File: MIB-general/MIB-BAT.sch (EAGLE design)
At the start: 19 parts, among them IC1 74LS14N, X1 MAB5SH, X2 MAB5SH

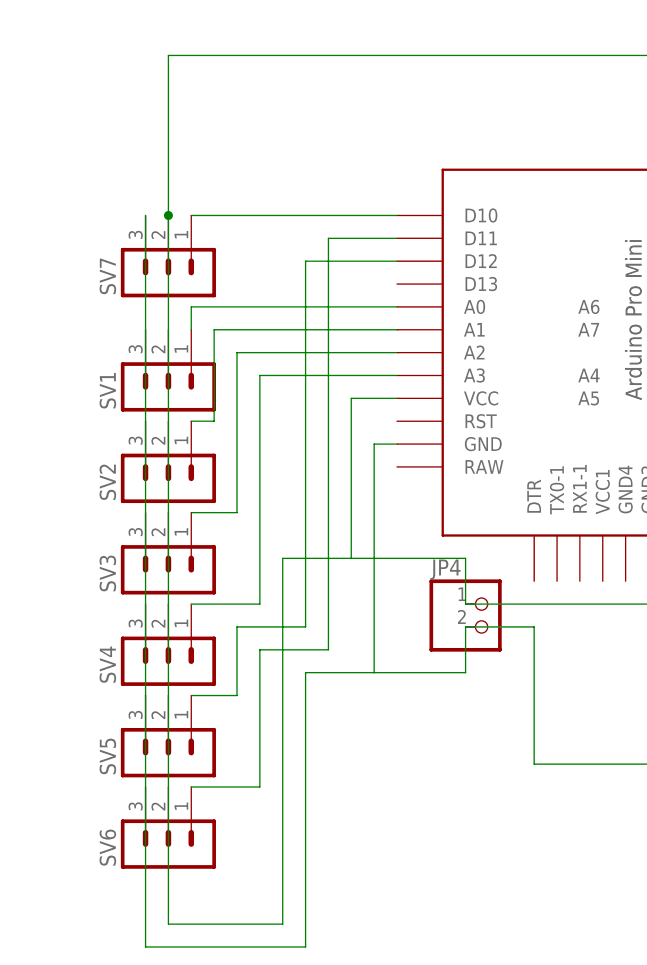
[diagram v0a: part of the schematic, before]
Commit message: Better version board with optional battery power supply
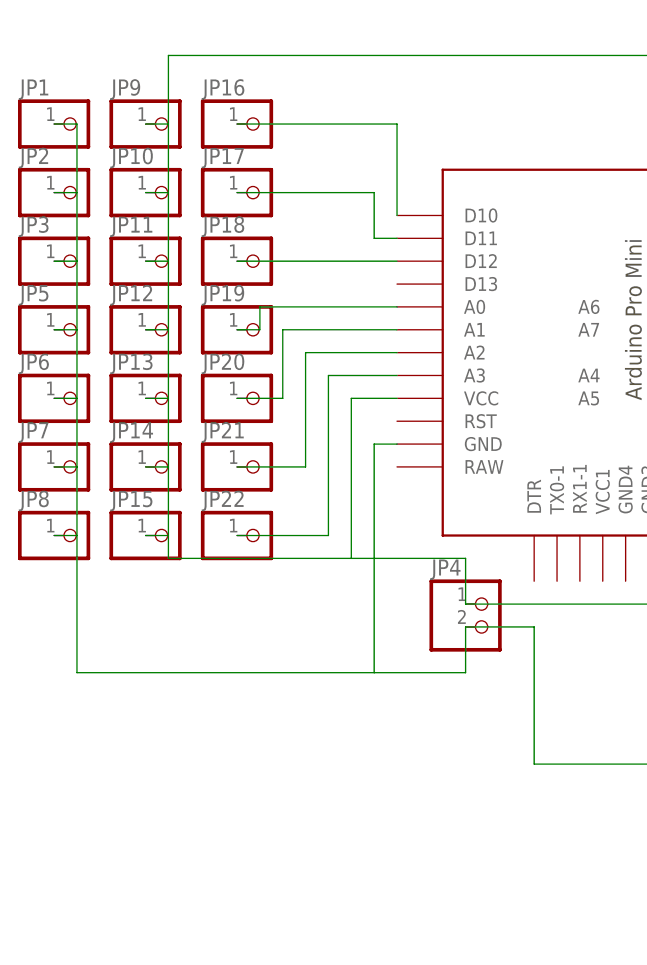
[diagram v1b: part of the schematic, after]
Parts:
- removed SV1, SV2, SV3, SV4, SV5, SV6, SV7: (no value), con-lstb:MA03-1
- added JP1, JP10, JP11, JP12, JP13, JP14, JP15, JP16, JP17, JP18, JP19, JP2, JP20, JP21, JP22, JP3, JP5, JP6, JP7, JP8, JP9: (no value), pinhead:PINHD-1X1
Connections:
- removed net N$9: IC1P.VCC, JP4.1, OK2.VCC, R2.1, R3.2, SV1.2, SV2.2, SV3.2, SV4.2, SV5.2, SV6.2, SV7.2, U$1.VCC
- new net N$29: JP21.1, U$1.A2
- net N$11: now also JP1.1, JP2.1, JP3.1, JP5.1, JP6.1, JP7.1, JP8.1; no longer SV1.3, SV2.3, SV3.3, SV4.3, SV5.3, SV6.3, SV7.3
- net N$13: now also JP16.1, U$1.D10; no longer SV2.1, U$1.A1
- net N$14: now also JP17.1, U$1.D11; no longer SV3.1, U$1.A2
- net N$15: now also IC1P.VCC, JP10.1, JP11.1, JP12.1, JP13.1, JP14.1, JP15.1, JP4.1, JP9.1, OK2.VCC, R2.1, R3.2, U$1.VCC; no longer SV4.1, U$1.A3
- net N$16: now also JP18.1, U$1.D12; no longer SV1.1, U$1.A0
- net N$18: now also JP19.1, U$1.A0; no longer SV5.1, U$1.D12
- net N$19: now also JP20.1, U$1.A1; no longer SV6.1, U$1.D11
- net N$30: now also JP22.1, U$1.A3; no longer SV7.1, U$1.D10

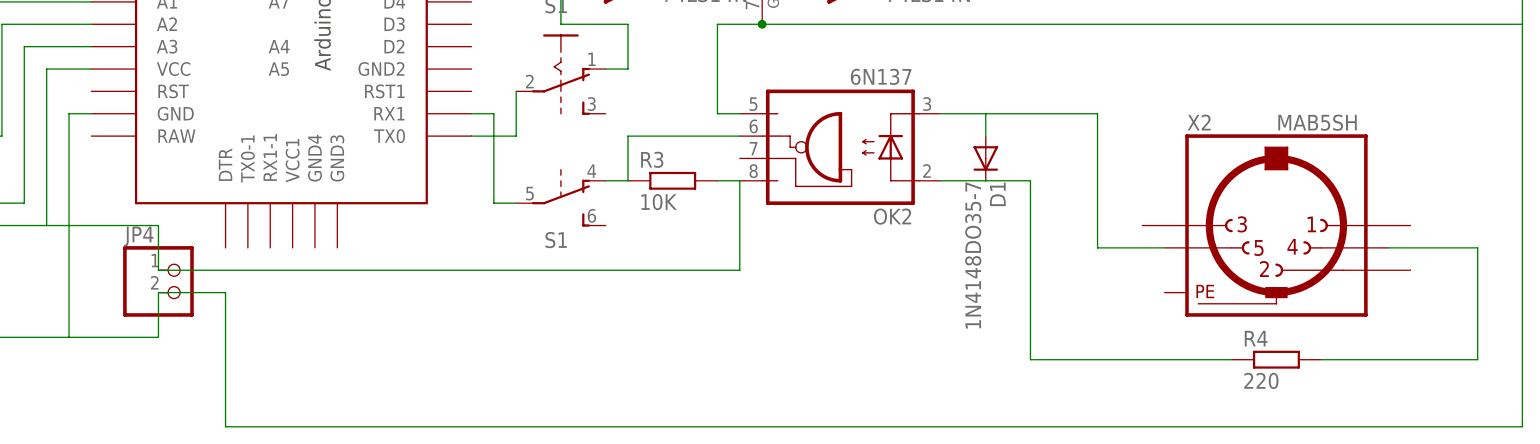
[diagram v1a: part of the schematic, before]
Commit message: New PCB layout enabling choice of optocoupler and makes the buffer optional.
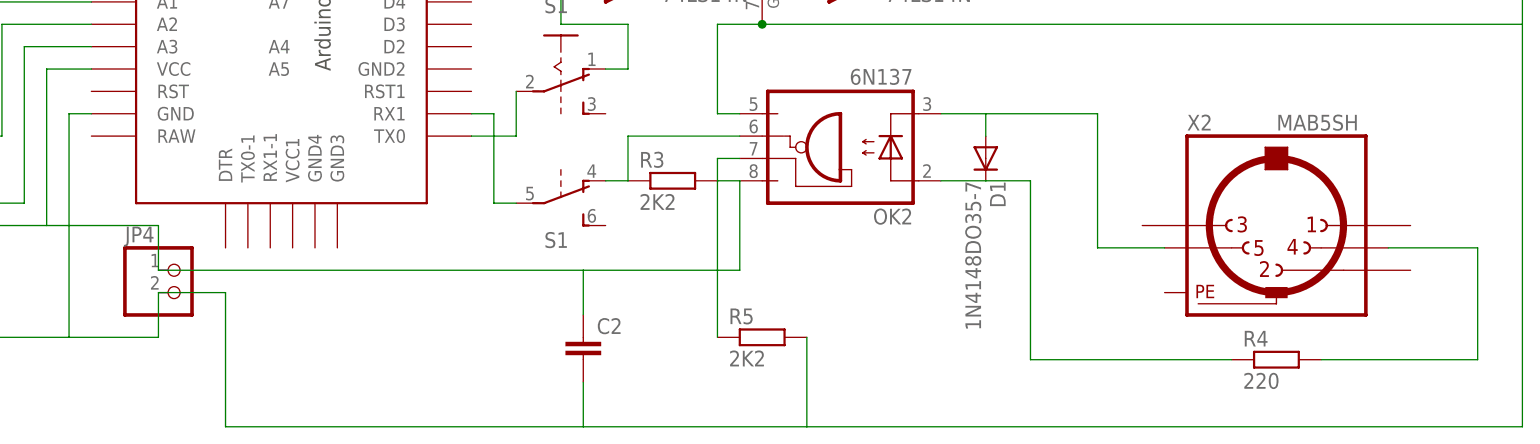
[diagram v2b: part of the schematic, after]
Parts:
- added C2: (no value), capacitor-wima:C7.5/3
- added R5: 2K2, rcl:R-EU_0207/10
- R3: value 10K -> 2K2
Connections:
- new net N$41: OK2.VE, R5.1
- net N$11: now also C2.2, R5.2
- net N$15: now also C2.1
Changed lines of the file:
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@@
 <part name="R1" library="rcl" deviceset="R-EU_" device="0207/10" value="220"/>
 <part name="R2" library="rcl" deviceset="R-EU_" device="0207/10" value="220"/>
-<part name="R3" library="rcl" deviceset="R-EU_" device="0207/10" value="10K"/>
+<part name="R3" library="rcl" deviceset="R-EU_" device="0207/10" value="2K2"/>
 <part name="R4" library="rcl" deviceset="R-EU_" device="0207/10" value="220"/>
 <part name="D1" library="diode" deviceset="1N4148" device="DO35-7"/>
@@
 <part name="JP21" library="pinhead" deviceset="PINHD-1X1" device=""/>
 <part name="JP22" library="pinhead" deviceset="PINHD-1X1" device=""/>
+<part name="C2" library="capacitor-wima" deviceset="C" device="7.5/3"/>
+<part name="R5" library="rcl" deviceset="R-EU_" device="0207/10" value="2K2"/>
 </parts>
 <sheets>
@@
 <instance part="JP21" gate="G$1" x="-7.62" y="40.64"/>
 <instance part="JP22" gate="G$1" x="-7.62" y="33.02"/>
+<instance part="C2" gate="G$1" x="63.5" y="17.78"/>
+<instance part="R5" gate="G$1" x="83.82" y="17.78"/>
 </instances>
 <busses>
@@
 <pinref part="X1" gate="G$1" pin="2"/>
 <wire x1="170.18" y1="53.34" x2="170.18" y2="7.62" width="0.1524" layer="91"/>
-<wire x1="170.18" y1="7.62" x2="22.86" y2="7.62" width="0.1524" layer="91"/>
+<wire x1="170.18" y1="7.62" x2="88.9" y2="7.62" width="0.1524" layer="91"/>
+<wire x1="88.9" y1="7.62" x2="63.5" y2="7.62" width="0.1524" layer="91"/>
+<wire x1="63.5" y1="7.62" x2="22.86" y2="7.62" width="0.1524" layer="91"/>
 <wire x1="22.86" y1="7.62" x2="22.86" y2="22.86" width="0.1524" layer="91"/>
 <wire x1="22.86" y1="22.86" x2="15.24" y2="22.86" width="0.1524" layer="91"/>
@@
 <pinref part="JP8" gate="G$1" pin="1"/>
 <wire x1="-30.48" y1="33.02" x2="-27.94" y2="33.02" width="0.1524" layer="91"/>
+<pinref part="C2" gate="G$1" pin="2"/>
+<wire x1="63.5" y1="12.7" x2="63.5" y2="7.62" width="0.1524" layer="91"/>
+<pinref part="R5" gate="G$1" pin="2"/>
+<wire x1="88.9" y1="17.78" x2="88.9" y2="7.62" width="0.1524" layer="91"/>
 </segment>
 </net>
@@
 </segment>
 </net>
-<net name="N$22" class="0">
+<net name="N$42" class="0">
 <segment>
 <pinref part="S1" gate="A" pin="O"/>
@@
 <wire x1="81.28" y1="25.4" x2="81.28" y2="35.56" width="0.1524" layer="91"/>
 <pinref part="JP4" gate="G$1" pin="1"/>
-<wire x1="15.24" y1="25.4" x2="81.28" y2="25.4" width="0.1524" layer="91"/>
+<wire x1="15.24" y1="25.4" x2="63.5" y2="25.4" width="0.1524" layer="91"/>
+<wire x1="63.5" y1="25.4" x2="81.28" y2="25.4" width="0.1524" layer="91"/>
 <wire x1="15.24" y1="25.4" x2="15.24" y2="30.48" width="0.1524" layer="91"/>
 <wire x1="-17.78" y1="30.48" x2="2.54" y2="30.48" width="0.1524" layer="91"/>
@@
 <pinref part="JP15" gate="G$1" pin="1"/>
 <wire x1="-20.32" y1="33.02" x2="-17.78" y2="33.02" width="0.1524" layer="91"/>
+<pinref part="C2" gate="G$1" pin="1"/>
+<wire x1="63.5" y1="20.32" x2="63.5" y2="25.4" width="0.1524" layer="91"/>
 </segment>
 </net>
@@
 </segment>
 </net>
+<net name="N$41" class="0">
+<segment>
+<pinref part="OK2" gate="A" pin="VE"/>
+<wire x1="81.28" y1="38.1" x2="78.74" y2="38.1" width="0.1524" layer="91"/>
+<pinref part="R5" gate="G$1" pin="1"/>
+<wire x1="78.74" y1="38.1" x2="78.74" y2="17.78" width="0.1524" layer="91"/>
+</segment>
+</net>
